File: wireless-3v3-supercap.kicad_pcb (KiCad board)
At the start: 2 copper layers, 88 x 40 mm, 13 parts, among them J1 POWER-OUT, J2 POWER-IN, SW1 MODE, U1 BQ24640RVAR, U2 TPS61022

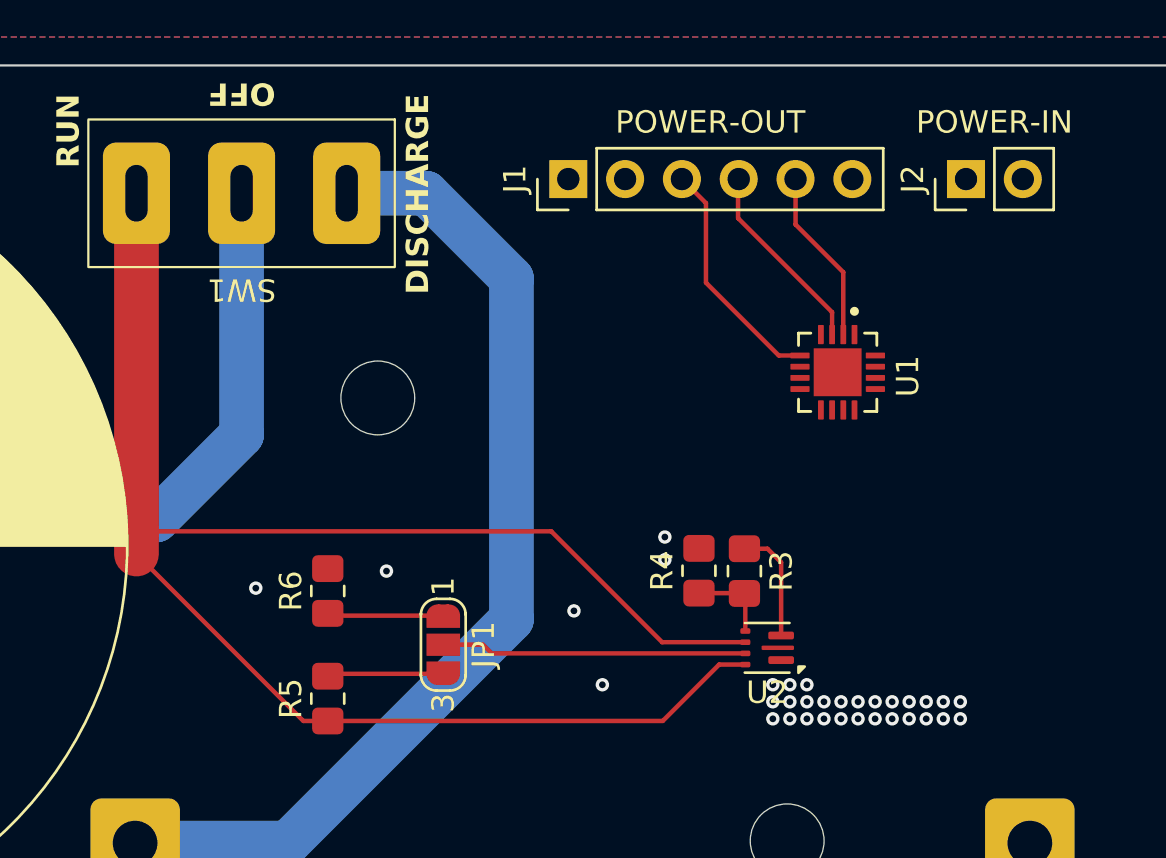
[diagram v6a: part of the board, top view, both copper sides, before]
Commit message: Add power output capacitors
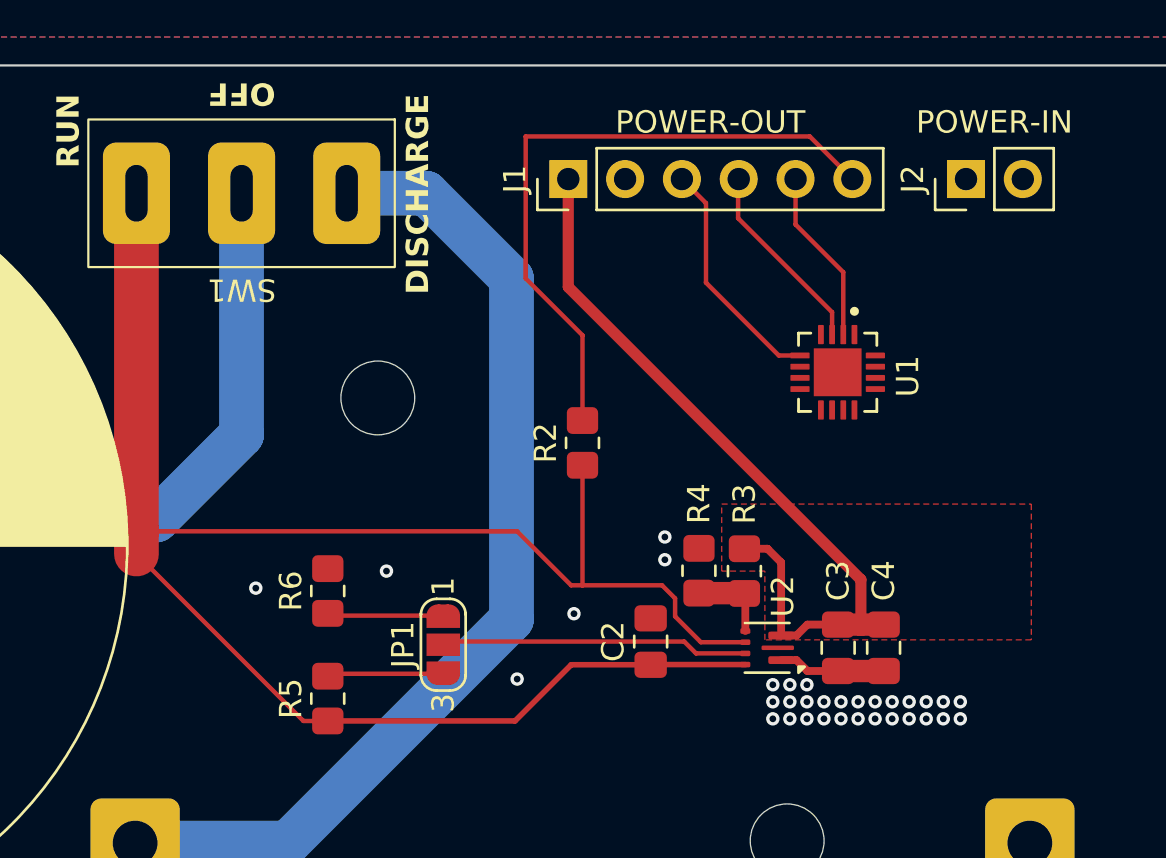
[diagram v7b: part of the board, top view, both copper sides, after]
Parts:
- added C2: 10µF X7R, Capacitor_SMD:C_0805_2012Metric_Pad1.18x1.45mm_HandSolder, F.Cu at (87.5, 51.2)
- added C3: 22µF X7R, Capacitor_SMD:C_0805_2012Metric_Pad1.18x1.45mm_HandSolder, F.Cu at (95.9, 51.4)
- added C4: 22µF X7R, Capacitor_SMD:C_0805_2012Metric_Pad1.18x1.45mm_HandSolder, F.Cu at (97.9, 51.4)
- added R2: 1kΩ 1% 125mW, Resistor_SMD:R_0805_2012Metric_Pad1.20x1.40mm_HandSolder, F.Cu at (84.5, 42.3)
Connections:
- net Net-(U2-FB) renamed /Power Out/POWER_FB
- net Net-(U2-SW) renamed /Power Out/POWER_SW
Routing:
- net +3.3V: track 5.16 -> 35.3 mm
- net CAPACITOR_VOLTAGE: track 0.00 -> 29.1 mm
- net /Charge/SUPERCAP: track 76.8 -> 82.6 mm
- net GND: track 0.00 -> 4.78 mm
- added copper zone on F.Cu, net +3.3V

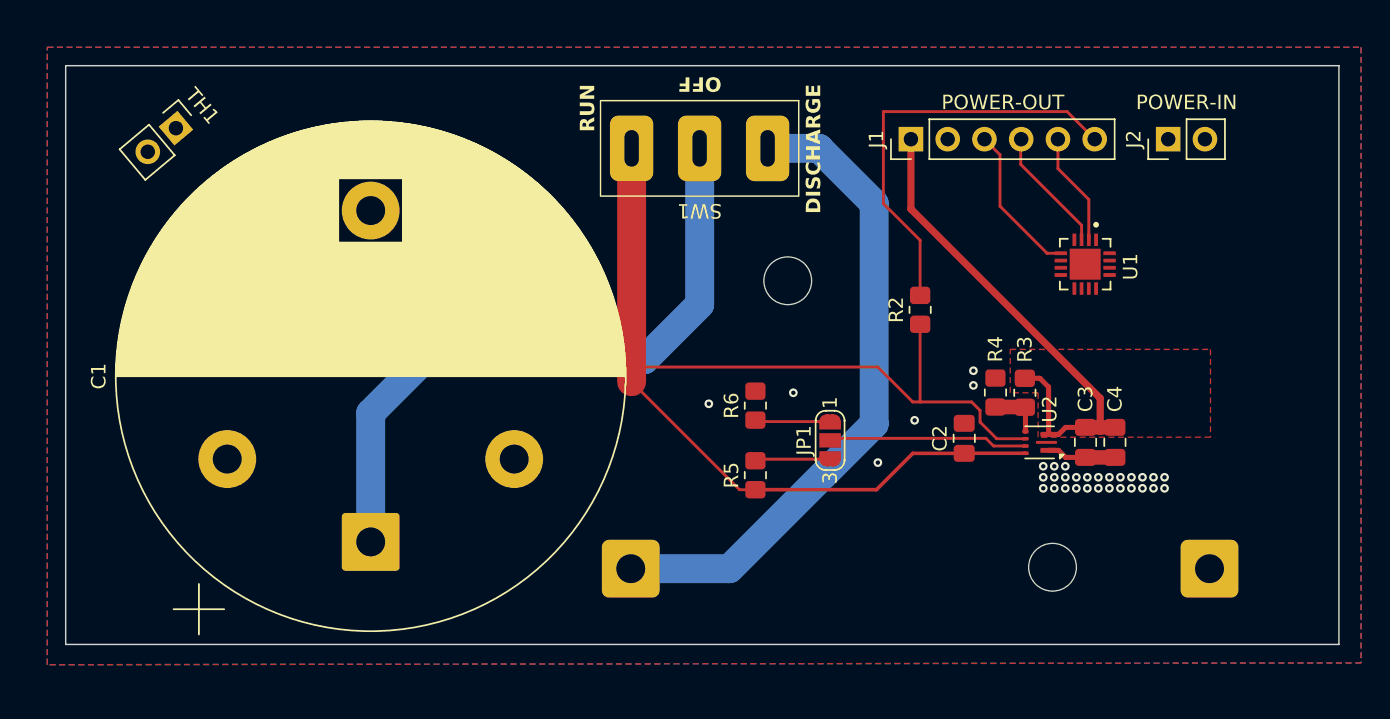
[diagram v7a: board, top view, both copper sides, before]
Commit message: Add inductor and finish power out layout
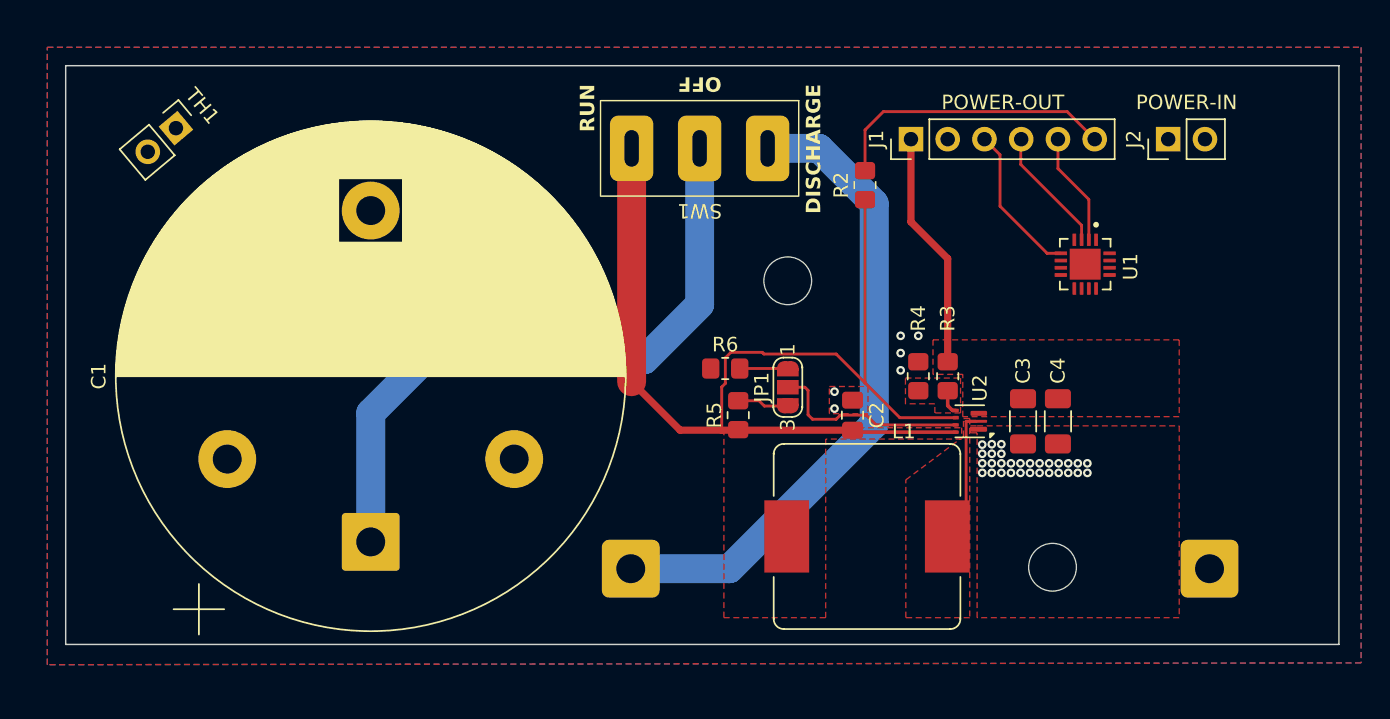
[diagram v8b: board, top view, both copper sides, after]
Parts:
- added L1: 1µH 25A 30%, Inductor_SMD:L_Bourns_SRP1245A, F.Cu at (80.8, 57.9)
- C2: value 10µF X7R -> 10µF 10% 10V X7R
- C3, C4: value 22µF X7R -> 22µF 10% 10V X7R; footprint Capacitor_SMD:C_0805_2012Metric_Pad1.18x1.45mm_HandSolder -> Capacitor_SMD:C_1206_3216Metric_Pad1.33x1.80mm_HandSolder
- moved R2 9.42 mm to (80.6, 33.7)
- moved C2 7.89 mm to (79.8, 49.6)
- moved R3 5.46 mm to (86.4, 46.9)
- moved R4 5.45 mm to (84.3, 46.9)
- moved U2 5.04 mm to (87.9, 50.0)
- moved JP1 4.69 mm to (75.3, 47.6)
- moved C3 4.56 mm to (91.6, 50.0)
- moved R5 4.32 mm to (71.9, 49.6)
- moved C4 4.20 mm to (94.0, 50.0)
- moved R6 3.31 mm to (71.0, 46.3), turned to 180 degrees
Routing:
- net +3.3V: track 35.3 -> 16.4 mm
- net CAPACITOR_VOLTAGE: track 29.1 -> 20.0 mm
- net /Power Out/POWER_SW: track 0.00 -> 7.39 mm
- net /Charge/SUPERCAP: track 82.6 -> 75.5 mm
- net GND: track 4.78 -> 0.00 mm, vias 33 -> 36
- net /Power Out/POWER_FB: track 3.73 -> 1.72 mm
- net Net-(JP1-A): track 5.21 -> 3.32 mm
- net Net-(JP1-B): track 5.21 -> 3.58 mm
- added copper zone on F.Cu, net /Charge/SUPERCAP
- added copper zone on F.Cu, net /Power Out/POWER_FB
- added copper zone on F.Cu, net /Power Out/POWER_SW
